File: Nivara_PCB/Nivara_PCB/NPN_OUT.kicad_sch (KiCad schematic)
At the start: 8 parts, among them Q1 IRLML0040, U8 LTV-357T

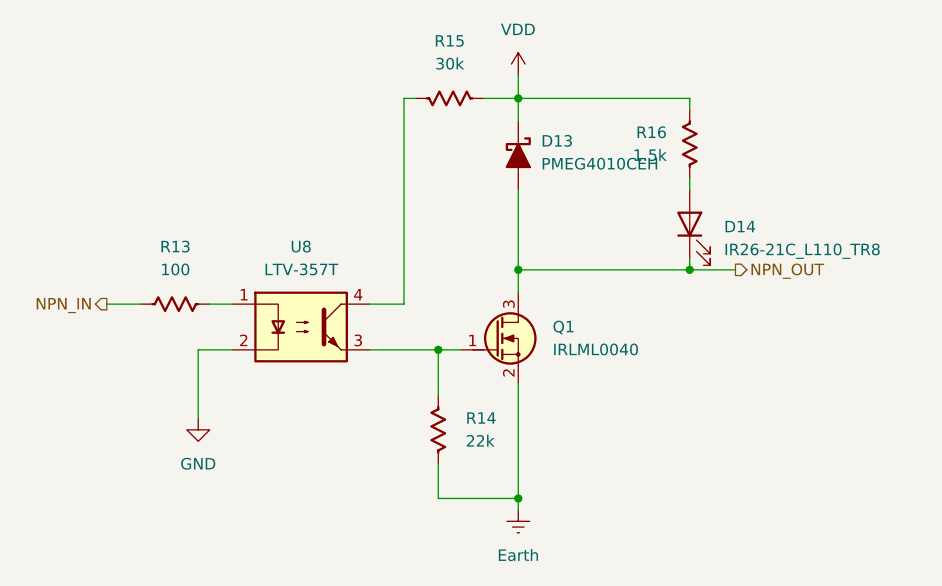
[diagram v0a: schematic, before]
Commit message: Cambios finales en la comprobación del DRC.
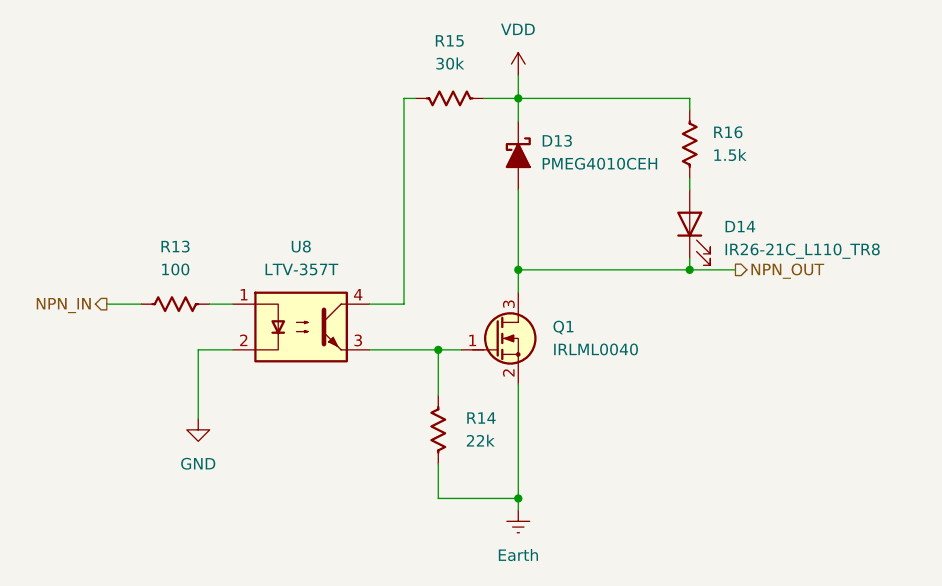
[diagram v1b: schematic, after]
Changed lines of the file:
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@@
 		(lib_id "EasyEDA:R_0603")
 		(at 125.73 72.39 0)
-		(mirror y)
 		(unit 1)
 		(exclude_from_sim no)
@@
 		(on_board yes)
 		(dnp no)
-		(fields_autoplaced yes)
 		(property "Reference" "R16"
-			(at 123.19 71.1199 0)
+			(at 128.27 71.1199 0)
 			(effects
 				(font
@@
 		)
 		(property "Value" "1.5k"
-			(at 123.19 73.6599 0)
+			(at 128.27 73.6599 0)
 			(effects
 				(font

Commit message: TERMINACIONES Y AJUSTES FINALES
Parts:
- removed D14: IR26-21C_L110_TR8, LED_SMD:LED_1206_3216Metric, symbol LED:IR26-21C_L110_TR8
- added D14: LED, LED_SMD:LED_0603_1608Metric, symbol EasyEDA:LED
- D13: LCSC Part (none) -> C193342; Part # (none) -> PMEG4010CEH,115
- Q1: LCSC Part (none) -> C5364305; Part # (none) -> IRLML0040
- R17: renamed from R13; LCSC Part (none) -> C22775; Part # (none) -> 0603WAF1000T5E
- R18: renamed from R14; LCSC Part (none) -> C31850; Part # (none) -> 0603WAF2202T5E
- R19: renamed from R15; LCSC Part (none) -> C22984; Part # (none) -> 0603WAF3002T5E
- R20: renamed from R16; LCSC Part (none) -> C22843; Part # (none) -> 0603WAF1501T5E
- U10: renamed from U8; LCSC Part (none) -> C119091; Part # (none) -> LTV-357T-C
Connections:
- net NPN_OUT: now also D14.1 (K)
- net at R20.2: now also D14.2 (A)
